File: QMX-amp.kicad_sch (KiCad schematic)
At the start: 0 parts

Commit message: PCB template now fits the QMX dead space
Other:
- company: (none) -> WA7GIL
- title: (none) -> QMX Amp
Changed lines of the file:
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@@
 	(generator "eeschema")
 	(generator_version "8.0")
-	(paper "A4")
+	(paper "USLetter")
 	(title_block
-		(date "2021-02-16")
+		(title "QMX Amp")
+		(date "2024-08-05")
+		(rev "v0.1")
+		(company "WA7GIL")
 	)
 	(sheet_instances

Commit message: starting working on schematic. struggling with relays
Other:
- added sheet LPF Relay Control (untitled.kicad_sch)
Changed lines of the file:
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@@
 		(company "WA7GIL")
+	)
+	(symbol
+		(lib_id "power:GND")
+		(at 105.41 30.48 270)
+		(unit 1)
+		(exclude_from_sim no)
+		(in_bom yes)
+		(on_board yes)
+		(dnp no)
+		(fields_autoplaced yes)
+		(property "Reference" "#PWR02"
+			(at 99.06 30.48 0)
+			(effects
+				(font
+					(size 1.27 1.27)
+				)
+				(hide yes)
+			)
+		)
+		(property "Value" "GND"
+			(at 101.6 30.4799 90)
+			(effects
+				(font
+					(size 1.27 1.27)
+				)
+				(justify right)
+			)
+		)
+		(property "Footprint" ""
+			(at 105.41 30.48 0)
+			(effects
+				(font
+					(size 1.27 1.27)
+				)
+				(hide yes)
+			)
+		)
+		(property "Datasheet" ""
+			(at 105.41 30.48 0)
+			(effects
+				(font
+					(size 1.27 1.27)
+				)
+				(hide yes)
+			)
+		)
+		(property "Description" "Power symbol creates a global label with name \"GND\" , ground"
+			(at 105.41 30.48 0)
+			(effects
+				(font
+					(size 1.27 1.27)
+				)
+				(hide yes)
+			)
+		)
+		(pin "1"
+		)
+		(instances
+			(project ""
+				(path "/e63e39d7-6ac0-4ffd-8aa3-1841a4541b55"
+					(reference "#PWR02")
+					(unit 1)
+				)
+			)
+		)
+	)
+	(symbol
+		(lib_id "power:+5V")
+		(at 105.41 25.4 90)
+		(unit 1)
+		(exclude_from_sim no)
+		(in_bom yes)
+		(on_board yes)
+		(dnp no)
+		(fields_autoplaced yes)
+		(property "Reference" "#PWR01"
+			(at 109.22 25.4 0)
+			(effects
+				(font
+					(size 1.27 1.27)
+				)
+				(hide yes)
+			)
+		)
+		(property "Value" "+5V"
+			(at 101.6 25.3999 90)
+			(effects
+				(font
+					(size 1.27 1.27)
+				)
+				(justify left)
+			)
+		)
+		(property "Footprint" ""
+			(at 105.41 25.4 0)
+			(effects
+				(font
+					(size 1.27 1.27)
+				)
+				(hide yes)
+			)
+		)
+		(property "Datasheet" ""
+			(at 105.41 25.4 0)
+			(effects
+				(font
+					(size 1.27 1.27)
+				)
+				(hide yes)
+			)
+		)
+		(property "Description" "Power symbol creates a global label with name \"+5V\""
+			(at 105.41 25.4 0)
+			(effects
+				(font
+					(size 1.27 1.27)
+				)
+				(hide yes)
+			)
+		)
+		(pin "1"
+		)
+		(instances
+			(project ""
+				(path "/e63e39d7-6ac0-4ffd-8aa3-1841a4541b55"
+					(reference "#PWR01")
+					(unit 1)
+				)
+			)
+		)
+	)
+	(sheet
+		(at 195.58 25.4)
+		(size 27.94 38.1)
+		(fields_autoplaced yes)
+		(stroke
+			(width 0.1524)
+			(type solid)
+		)
+		(fill
+			(color 0 0 0 0.0000)
+		)
+		(property "Sheetname" "LPF Relay Control"
+			(at 195.58 24.6884 0)
+			(effects
+				(font
+					(size 1.27 1.27)
+				)
+				(justify left bottom)
+			)
+		)
+		(property "Sheetfile" "untitled.kicad_sch"
+			(at 195.58 64.0846 0)
+			(effects
+				(font
+					(size 1.27 1.27)
+				)
+				(justify left top)
+			)
+		)
+		(pin "+3.3V control from QMX+" bidirectional
+			(at 195.58 31.75 180)
+			(effects
+				(font
+					(size 1.27 1.27)
+				)
+				(justify left)
+			)
+		)
+		(instances
+			(project "QMX-amp"
+				(path "/e63e39d7-6ac0-4ffd-8aa3-1841a4541b55"
+					(page "2")
+				)
+			)
+		)
 	)
 	(sheet_instances

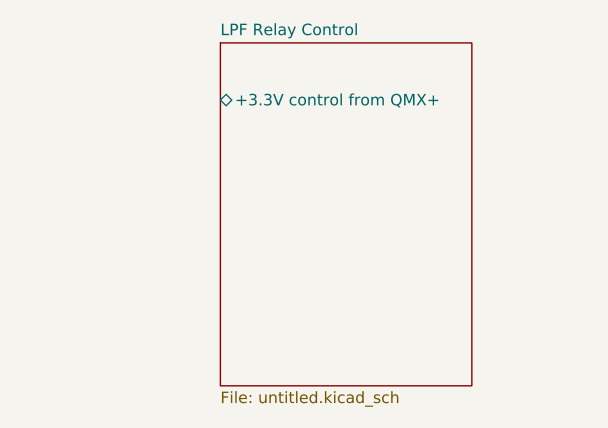
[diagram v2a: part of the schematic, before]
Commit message: made some progress on LPF Relay Control sheet.  Looks like it will span two sheets
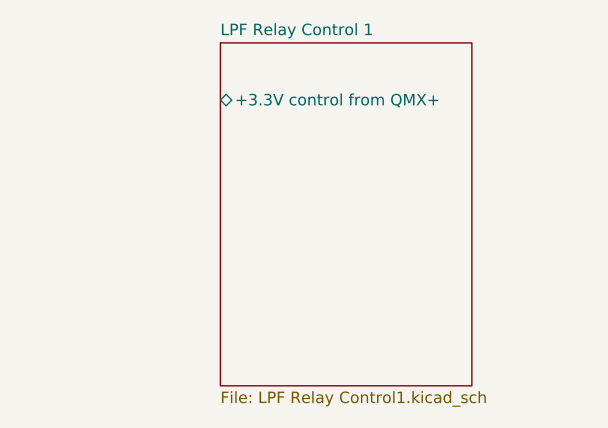
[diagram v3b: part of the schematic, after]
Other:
- sheet LPF Relay Control renamed LPF Relay Control 1
- sheet LPF Relay Control 1: file untitled.kicad_sch -> LPF Relay Control1.kicad_sch
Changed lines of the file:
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@@
 			(color 0 0 0 0.0000)
 		)
-		(property "Sheetname" "LPF Relay Control"
+		(property "Sheetname" "LPF Relay Control 1"
 			(at 195.58 24.6884 0)
 			(effects
@@
 			)
 		)
-		(property "Sheetfile" "untitled.kicad_sch"
+		(property "Sheetfile" "LPF Relay Control1.kicad_sch"
 			(at 195.58 64.0846 0)
 			(effects

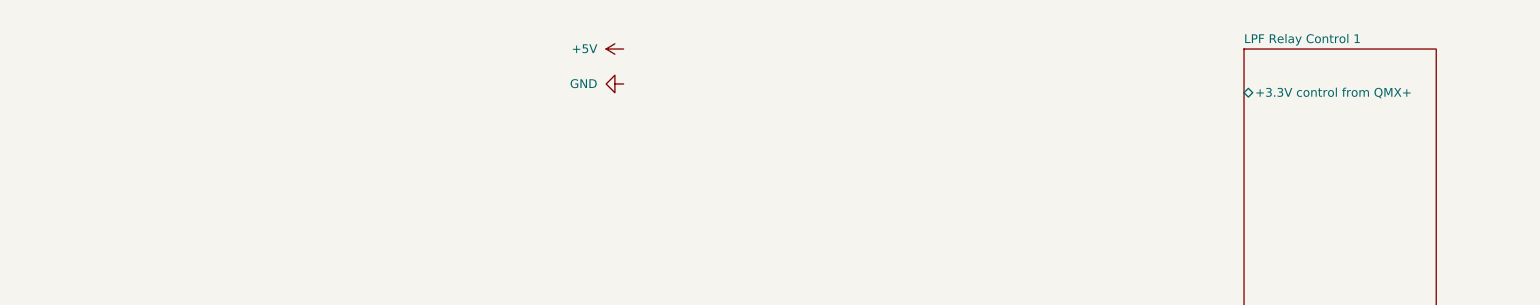
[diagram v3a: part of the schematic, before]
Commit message: Working on LPF control and actual filters.  They are intertwingled pretty tightly.  Also ran ERC and beat out some errors.
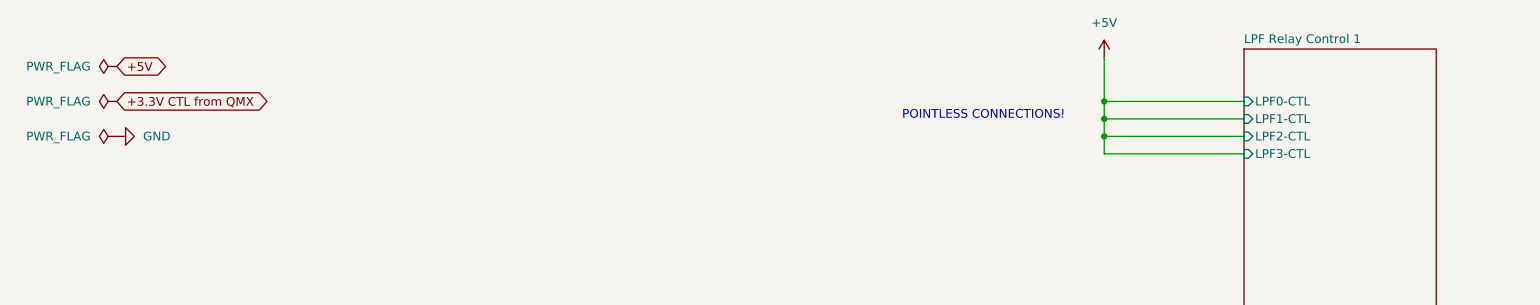
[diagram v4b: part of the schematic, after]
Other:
- sheet LPF Relay Control 1 ports: added LPF0-CTL, LPF1-CTL, LPF2-CTL, LPF3-CTL; removed +3.3V control from QMX+
- note added: "POINTLESS CONNECTIONS!"

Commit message: checkpoint progress, working on LPF chains
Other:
- note added: "Power and Ground"
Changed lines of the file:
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@@
+		)
+	)
+	(rectangle
+		(start 16.51 22.86)
+		(end 60.96 54.61)
+		(stroke
+			(width 0)
+			(type default)
+		)
+		(fill
+			(type none)
+		)
+	)
+	(text "Power and Ground"
+		(exclude_from_sim no)
+		(at 38.1 21.844 0)
+		(effects
+			(font
+				(size 1.27 1.27)
+			)
 		)
 	)

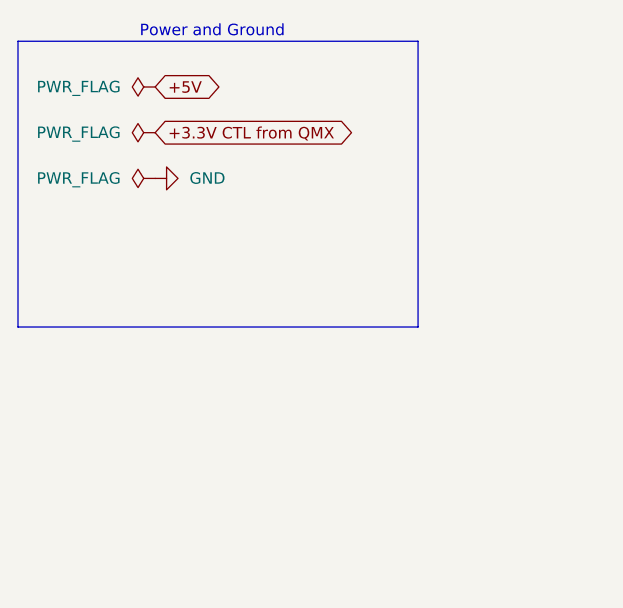
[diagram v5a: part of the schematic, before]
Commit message: added RF through LPF chains
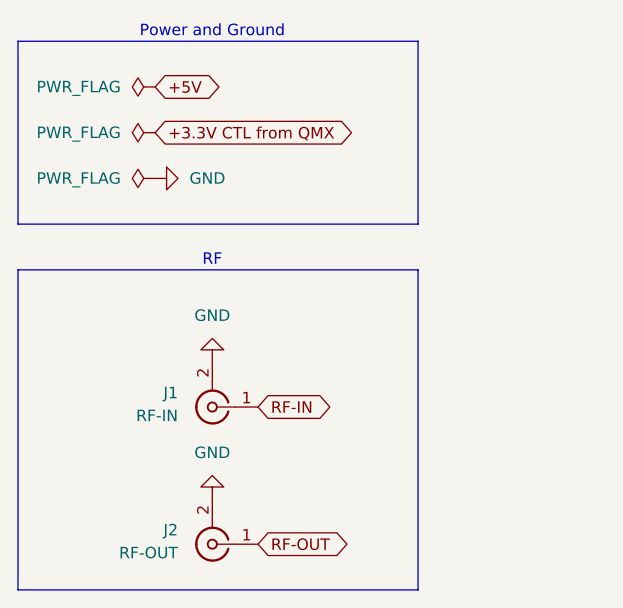
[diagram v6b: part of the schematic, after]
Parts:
- added J1: RF-IN, symbol Connector:Conn_Coaxial
- added J2: RF-OUT, symbol Connector:Conn_Coaxial
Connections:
- net GND: now also J1.2 (Ext), J2.2 (Ext)
- new net RF-IN: J1.1 (In)
- new net RF-OUT: J2.1 (In)
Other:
- note added: "RF"

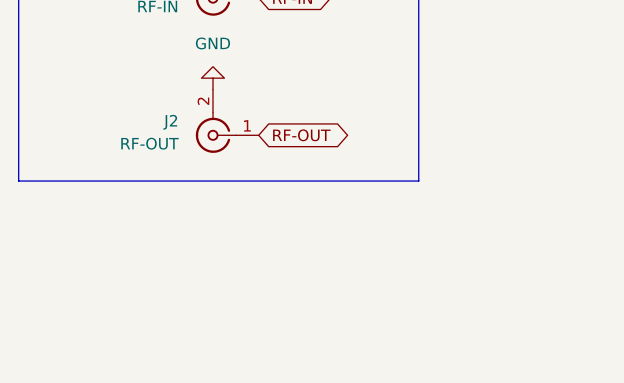
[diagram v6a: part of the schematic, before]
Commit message: worked on strange stuff on btm of LPF filter chain schematic.  ERC passes
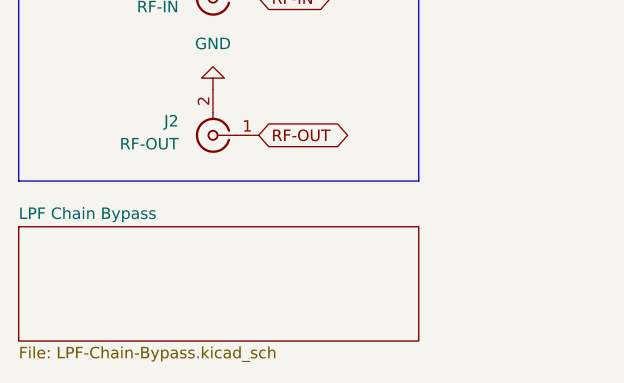
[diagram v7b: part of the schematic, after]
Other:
- added sheet LPF Chain Bypass (LPF-Chain-Bypass.kicad_sch)
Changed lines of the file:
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@@
+	)
+	(sheet
+		(at 16.51 88.9)
+		(size 44.45 12.7)
+		(fields_autoplaced yes)
+		(stroke
+			(width 0.1524)
+			(type solid)
+		)
+		(fill
+			(color 0 0 0 0.0000)
+		)
+		(property "Sheetname" "LPF Chain Bypass"
+			(at 16.51 88.1884 0)
+			(effects
+				(font
+					(size 1.27 1.27)
+				)
+				(justify left bottom)
+			)
+		)
+		(property "Sheetfile" "LPF-Chain-Bypass.kicad_sch"
+			(at 16.51 102.1846 0)
+			(effects
+				(font
+					(size 1.27 1.27)
+				)
+				(justify left top)
+			)
+		)
+		(instances
+			(project "QMX-amp"
+				(path "/e63e39d7-6ac0-4ffd-8aa3-1841a4541b55"
+					(page "4")
+				)
+			)
+		)
 	)
 	(sheet

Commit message: last of v0.1.  Ron stopped by with many corrections for me
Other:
- added sheet power (power.kicad_sch)
- moved on the sheet: J1, J2
